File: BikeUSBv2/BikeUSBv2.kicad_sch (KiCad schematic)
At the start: 50 parts, among them J1 TYPE-C-31-M-16, J2 Conn_01x02_Female, Q1 Q_NPN_BEC, SW1 SW_Push, SW2 SW_Push, U1 TPS63020DSJR, U2 ATtiny1616-M

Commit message: oops 2
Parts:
- D4, D5, D6, D7: footprint Diode_SMD:D_PowerDI-123 -> Diode_SMD:D_SOD-128
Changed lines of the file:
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@@
       (effects (font (size 1.27 1.27)) (justify left) hide)
     )
-    (property "Footprint" "Diode_SMD:D_PowerDI-123" (at 23.495 84.455 0)
+    (property "Footprint" "Diode_SMD:D_SOD-128" (at 23.495 84.455 0)
       (effects (font (size 1.27 1.27)) hide)
     )
@@
       (effects (font (size 1.27 1.27)) (justify left) hide)
     )
-    (property "Footprint" "Diode_SMD:D_PowerDI-123" (at 35.56 92.075 0)
+    (property "Footprint" "Diode_SMD:D_SOD-128" (at 35.56 92.075 0)
       (effects (font (size 1.27 1.27)) hide)
     )
@@
       (effects (font (size 1.27 1.27)) (justify left) hide)
     )
-    (property "Footprint" "Diode_SMD:D_PowerDI-123" (at 23.495 92.075 0)
+    (property "Footprint" "Diode_SMD:D_SOD-128" (at 23.495 92.075 0)
       (effects (font (size 1.27 1.27)) hide)
     )
@@
       (effects (font (size 1.27 1.27)) (justify left) hide)
     )
-    (property "Footprint" "Diode_SMD:D_PowerDI-123" (at 35.56 84.455 0)
-      (effects (font (size 1.27 1.27)) hide)
-    )
+    (property "Footprint" "Diode_SMD:D_SOD-128" (at 35.56 84.455 0)
+      (effects (font (size 1.27 1.27)) hide)
+    )

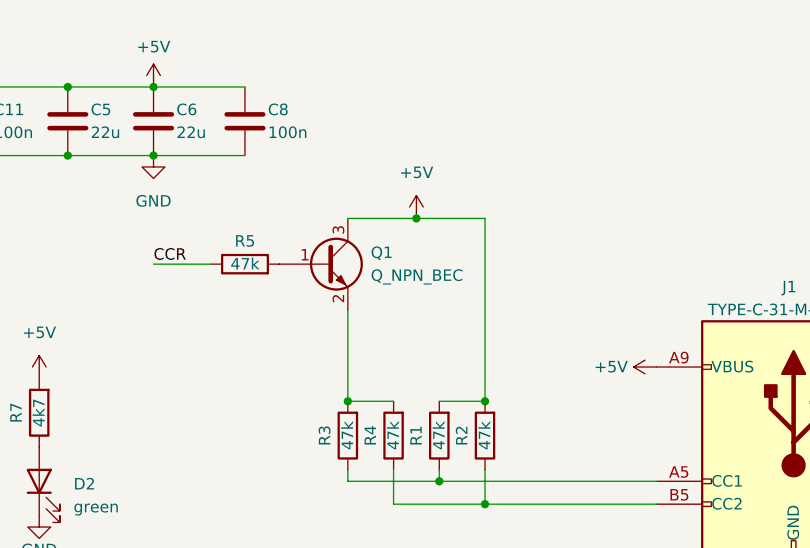
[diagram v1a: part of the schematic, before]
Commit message: NPN =/= PNP
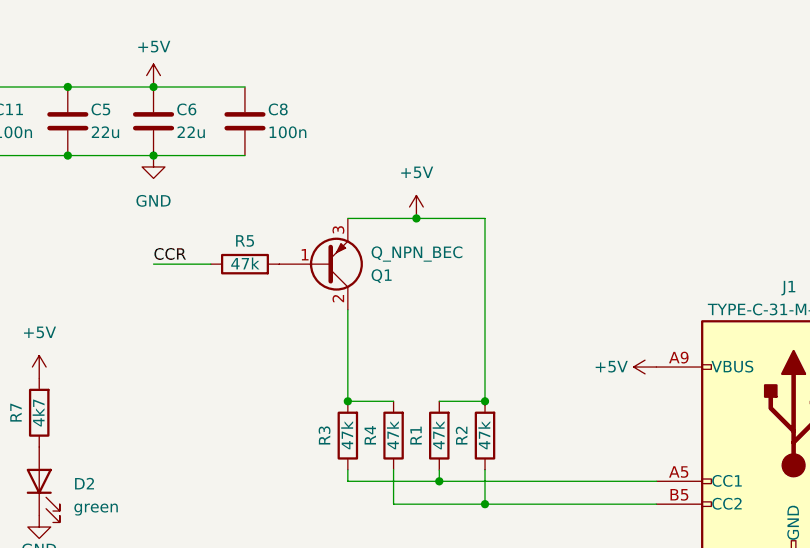
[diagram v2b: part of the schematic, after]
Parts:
- Q1: symbol Device:Q_NPN_BEC -> Device:Q_PNP_BCE
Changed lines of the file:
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@@
     )
   )
-  (symbol (lib_id "Device:Q_NPN_BEC") (at 157.48 73.66 0) (unit 1)
-    (in_bom yes) (on_board yes) (dnp no) (fields_autoplaced)
-    (property "Reference" "Q1" (at 162.56 72.39 0)
+  (symbol (lib_id "Device:Q_PNP_BCE") (at 157.48 73.66 0) (mirror x) (unit 1)
+    (in_bom yes) (on_board yes) (dnp no)
+    (property "Reference" "Q1" (at 162.56 74.93 0)
       (effects (font (size 1.27 1.27)) (justify left))
     )
-    (property "Value" "Q_NPN_BEC" (at 162.56 74.93 0)
+    (property "Value" "Q_NPN_BEC" (at 162.56 72.39 0)
       (effects (font (size 1.27 1.27)) (justify left))
     )
-    (property "Footprint" "Package_TO_SOT_SMD:SOT-23_Handsoldering" (at 162.56 71.12 0)
+    (property "Footprint" "Package_TO_SOT_SMD:SOT-23_Handsoldering" (at 162.56 76.2 0)
       (effects (font (size 1.27 1.27)) hide)
     )

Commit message: update parts
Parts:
- C1, C10, C11, C8: LCSC (none) -> C1711
- C2, C3, C4: LCSC (none) -> C1779
- C5, C6, C7: LCSC (none) -> C12891
- C9: LCSC (none) -> C178661
- D4, D5, D6, D7: LCSC (none) -> C603062
- D8: LCSC (none) -> C7422622
- J1: LCSC (none) -> C283541
- L1: LCSC (none) -> C338840
- Q1: value Q_NPN_BEC -> MMBT3906; LCSC (none) -> C2891809; LCSC Part (none) -> C2891809
- R1, R10, R11, R2, R3, R4, R5: LCSC (none) -> C218592
- R12, R13, R14, R7, R8, R9: LCSC (none) -> C706357
- U1: LCSC (none) -> C15483
- U2: LCSC (none) -> C507118
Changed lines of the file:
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@@
+      (effects (font (size 1.27 1.27)) hide)
+    )
+    (property "LCSC" "C218592" (at 148.59 71.12 0)
       (effects (font (size 1.27 1.27)) hide)
     )
@@
       (effects (font (size 1.27 1.27)) hide)
     )
+    (property "LCSC" "C706357" (at 24.13 121.92 0)
+      (effects (font (size 1.27 1.27)) hide)
+    )
     (pin "1")
     (pin "2")
@@
       (effects (font (size 1.27 1.27)) hide)
     )
+    (property "LCSC" "C706357" (at 80.645 181.61 0)
+      (effects (font (size 1.27 1.27)) hide)
+    )
     (pin "1")
     (pin "2")
@@
       (effects (font (size 1.27 1.27)) (justify left))
     )
-    (property "Value" "Q_NPN_BEC" (at 162.56 72.39 0)
+    (property "Value" "MMBT3906" (at 162.56 72.39 0)
       (effects (font (size 1.27 1.27)) (justify left))
     )
@@
     )
     (property "Datasheet" "~" (at 157.48 73.66 0)
+      (effects (font (size 1.27 1.27)) hide)
+    )
+    (property "LCSC Part" "C2891809" (at 157.48 73.66 0)
+      (effects (font (size 1.27 1.27)) hide)
+    )
+    (property "LCSC" "C2891809" (at 162.56 74.93 0)
       (effects (font (size 1.27 1.27)) hide)
     )
@@
       (effects (font (size 1.27 1.27)) hide)
     )
+    (property "LCSC" "C603062" (at 25.4 84.455 0)
+      (effects (font (size 1.27 1.27)) hide)
+    )
     (pin "2")
     (pin "1")
@@
       (effects (font (size 1.27 1.27)) hide)
     )
+    (property "LCSC" "C7422622" (at 22.86 54.61 0)
+      (effects (font (size 1.27 1.27)) hide)
+    )
     (pin "1")
     (pin "2")
@@
     )
     (property "Sim.Pins" "1=K 2=A" (at 35.56 92.075 0)
+      (effects (font (size 1.27 1.27)) hide)
+    )
+    (property "LCSC" "C603062" (at 31.115 92.075 0)
       (effects (font (size 1.27 1.27)) hide)
     )
@@
       (effects (font (size 1.27 1.27)) hide)
     )
+    (property "LCSC" "C1711" (at 120.65 56.515 0)
+      (effects (font (size 1.27 1.27)) hide)
+    )
     (pin "1")
     (pin "2")
@@
     )
     (property "Datasheet" "https://www.usb.org/sites/default/files/documents/usb_type-c.zip" (at 209.55 92.71 0)
+      (effects (font (size 1.27 1.27)) hide)
+    )
+    (property "LCSC" "C283541" (at 208.28 76.2 0)
       (effects (font (size 1.27 1.27)) hide)
     )
@@
       (effects (font (size 1.27 1.27)) hide)
     )
+    (property "LCSC" "C1711" (at 55.245 95.25 0)
+      (effects (font (size 1.27 1.27)) hide)
+    )
     (pin "1")
     (pin "2")
@@
     )
     (property "Datasheet" "~" (at 77.47 118.745 0)
+      (effects (font (size 1.27 1.27)) hide)
+    )
+    (property "LCSC" "C218592" (at 74.93 118.745 0)
       (effects (font (size 1.27 1.27)) hide)
     )
@@
       (effects (font (size 1.27 1.27)) hide)
     )
+    (property "LCSC" "C1711" (at 66.04 59.69 0)
+      (effects (font (size 1.27 1.27)) hide)
+    )
     (pin "1")
     (pin "2")
@@
       (effects (font (size 1.27 1.27)) hide)
     )
+    (property "LCSC" "C603062" (at 25.4 92.075 0)
+      (effects (font (size 1.27 1.27)) hide)
+    )
     (pin "2")
     (pin "1")
@@
       (effects (font (size 1.27 1.27)) hide)
     )
+    (property "LCSC" "C1711" (at 151.13 56.515 0)
+      (effects (font (size 1.27 1.27)) hide)
+    )
     (pin "1")
     (pin "2")
@@
       (effects (font (size 1.27 1.27)) hide)
     )
+    (property "LCSC" "C218592" (at 157.48 92.71 0)
+      (effects (font (size 1.27 1.27)) hide)
+    )
     (pin "1")
     (pin "2")
@@
       (effects (font (size 1.27 1.27)) hide)
     )
+    (property "LCSC" "C706357" (at 80.645 173.99 0)
+      (effects (font (size 1.27 1.27)) hide)
+    )
     (pin "1")
     (pin "2")
@@
       (effects (font (size 1.27 1.27)) hide)
     )
+    (property "LCSC" "C338840" (at 74.295 97.79 0)
+      (effects (font (size 1.27 1.27)) hide)
+    )
     (pin "1")
     (pin "2")
@@
       (effects (font (size 1.27 1.27)) hide)
     )
+    (property "LCSC" "C218592" (at 172.72 92.71 0)
+      (effects (font (size 1.27 1.27)) hide)
+    )
     (pin "1")
     (pin "2")
@@
       (effects (font (size 1.27 1.27)) hide)
     )
+    (property "LCSC" "C12891" (at 131.445 56.515 0)
+      (effects (font (size 1.27 1.27)) hide)
+    )
     (pin "1")
     (pin "2")
@@
       (effects (font (size 1.27 1.27)) hide)
     )
+    (property "LCSC" "C218592" (at 162.56 92.71 0)
+      (effects (font (size 1.27 1.27)) hide)
+    )
     (pin "1")
     (pin "2")
@@
     )
     (property "Datasheet" "~" (at 101.6 60.96 0)
+      (effects (font (size 1.27 1.27)) hide)
+    )
+    (property "LCSC" "C12891" (at 105.41 59.69 0)
       (effects (font (size 1.27 1.27)) hide)
     )
@@
     )
     (property "LCSC Part" "C15483" (at 93.345 120.015 0)
+      (effects (font (size 1.27 1.27)) hide)
+    )
+    (property "LCSC" "C15483" (at 93.345 76.835 0)
       (effects (font (size 1.27 1.27)) hide)
     )
@@
     )
     (property "Datasheet" "http://ww1.microchip.com/downloads/en/DeviceDoc/ATtiny3216_ATtiny1616-data-sheet-40001997B.pdf" (at 55.88 163.83 0)
+      (effects (font (size 1.27 1.27)) hide)
+    )
+    (property "LCSC" "C507118" (at 58.0741 138.43 0)
       (effects (font (size 1.27 1.27)) hide)
     )
@@
       (effects (font (size 1.27 1.27)) hide)
     )
+    (property "LCSC" "C1779" (at 85.09 59.69 0)
+      (effects (font (size 1.27 1.27)) hide)
+    )
     (pin "1")
     (pin "2")
@@
       (effects (font (size 1.27 1.27)) hide)
     )
+    (property "LCSC" "C218592" (at 114.3 86.995 0)
+      (effects (font (size 1.27 1.27)) hide)
+    )
     (pin "1")
     (pin "2")
@@
       (effects (font (size 1.27 1.27)) hide)
     )
+    (property "LCSC" "C706357" (at 74.93 126.365 0)
+      (effects (font (size 1.27 1.27)) hide)
+    )
     (pin "1")
     (pin "2")
@@
     )
     (property "Datasheet" "~" (at 116.84 94.615 0)
+      (effects (font (size 1.27 1.27)) hide)
+    )
+    (property "LCSC" "C706357" (at 114.3 94.615 0)
       (effects (font (size 1.27 1.27)) hide)
     )
@@
     )
     (property "Sim.Pins" "1=K 2=A" (at 35.56 84.455 0)
+      (effects (font (size 1.27 1.27)) hide)
+    )
+    (property "LCSC" "C603062" (at 31.115 84.455 0)
       (effects (font (size 1.27 1.27)) hide)
     )
@@
       (effects (font (size 1.27 1.27)) hide)
     )
+    (property "LCSC" "C1779" (at 75.565 59.69 0)
+      (effects (font (size 1.27 1.27)) hide)
+    )
     (pin "1")
     (pin "2")
@@
       (effects (font (size 1.27 1.27)) hide)
     )
+    (property "LCSC" "C706357" (at 123.19 90.17 0)
+      (effects (font (size 1.27 1.27)) hide)
+    )
     (pin "1")
     (pin "2")
@@
     )
     (property "Datasheet" "~" (at 138.43 57.785 0)
+      (effects (font (size 1.27 1.27)) hide)
+    )
+    (property "LCSC" "C12891" (at 140.97 56.515 0)
       (effects (font (size 1.27 1.27)) hide)
     )
@@
       (effects (font (size 1.27 1.27)) hide)
     )
+    (property "LCSC" "C178661" (at 48.26 70.231 0)
+      (effects (font (size 1.27 1.27)) hide)
+    )
     (pin "1")
     (pin "2")
@@
       (effects (font (size 1.27 1.27)) hide)
     )
+    (property "LCSC" "C218592" (at 167.64 92.71 0)
+      (effects (font (size 1.27 1.27)) hide)
+    )
     (pin "1")
     (pin "2")
@@
       (effects (font (size 1.27 1.27)) hide)
     )
+    (property "LCSC" "C1779" (at 94.615 59.69 0)
+      (effects (font (size 1.27 1.27)) hide)
+    )

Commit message: dingsbumbs
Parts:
- C1, C10, C11, C8: LCSC C1711 -> (none)
- C2, C3, C4: LCSC C1779 -> (none)
- C5, C6, C7: LCSC C12891 -> (none)
- C9: LCSC C178661 -> (none)
- D10: value CMS04(TE12L,Q,M) -> ~
- D4, D5, D6, D7: LCSC C603062 -> (none)
- D8: LCSC C7422622 -> (none)
- J1: LCSC C283541 -> (none)
- L1: LCSC C338840 -> (none)
- Q1: LCSC C2891809 -> (none)
- R1, R10, R11, R2, R3, R4, R5: LCSC C218592 -> (none)
- R12, R13, R14, R7, R8, R9: LCSC C706357 -> (none)
- U1: LCSC C15483 -> (none)
- U2: LCSC C507118 -> (none)
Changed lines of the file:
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@@
-      (effects (font (size 1.27 1.27)) hide)
-    )
-    (property "LCSC" "C218592" (at 148.59 71.12 0)
       (effects (font (size 1.27 1.27)) hide)
     )
@@
       (effects (font (size 1.27 1.27)) hide)
     )
-    (property "LCSC" "C706357" (at 24.13 121.92 0)
-      (effects (font (size 1.27 1.27)) hide)
-    )
     (pin "1")
     (pin "2")
@@
       (effects (font (size 1.27 1.27)) (justify left))
     )
-    (property "Value" "CMS04(TE12L,Q,M)" (at 81.915 127.635 90)
+    (property "Value" "~" (at 81.915 127.635 90)
       (effects (font (size 1.27 1.27)) (justify left) hide)
     )
@@
       (effects (font (size 1.27 1.27)) hide)
     )
-    (property "LCSC" "C706357" (at 80.645 181.61 0)
-      (effects (font (size 1.27 1.27)) hide)
-    )
     (pin "1")
     (pin "2")
@@
     )
     (property "LCSC Part" "C2891809" (at 157.48 73.66 0)
-      (effects (font (size 1.27 1.27)) hide)
-    )
-    (property "LCSC" "C2891809" (at 162.56 74.93 0)
       (effects (font (size 1.27 1.27)) hide)
     )
@@
       (effects (font (size 1.27 1.27)) hide)
     )
-    (property "LCSC" "C603062" (at 25.4 84.455 0)
-      (effects (font (size 1.27 1.27)) hide)
-    )
     (pin "2")
     (pin "1")
@@
       (effects (font (size 1.27 1.27)) hide)
     )
-    (property "LCSC" "C7422622" (at 22.86 54.61 0)
-      (effects (font (size 1.27 1.27)) hide)
-    )
     (pin "1")
     (pin "2")
@@
     )
     (property "Sim.Pins" "1=K 2=A" (at 35.56 92.075 0)
-      (effects (font (size 1.27 1.27)) hide)
-    )
-    (property "LCSC" "C603062" (at 31.115 92.075 0)
       (effects (font (size 1.27 1.27)) hide)
     )
@@
       (effects (font (size 1.27 1.27)) hide)
     )
-    (property "LCSC" "C1711" (at 120.65 56.515 0)
-      (effects (font (size 1.27 1.27)) hide)
-    )
     (pin "1")
     (pin "2")
@@
     )
     (property "Datasheet" "https://www.usb.org/sites/default/files/documents/usb_type-c.zip" (at 209.55 92.71 0)
-      (effects (font (size 1.27 1.27)) hide)
-    )
-    (property "LCSC" "C283541" (at 208.28 76.2 0)
       (effects (font (size 1.27 1.27)) hide)
     )
@@
       (effects (font (size 1.27 1.27)) hide)
     )
-    (property "LCSC" "C1711" (at 55.245 95.25 0)
-      (effects (font (size 1.27 1.27)) hide)
-    )
     (pin "1")
     (pin "2")
@@
     )
     (property "Datasheet" "~" (at 77.47 118.745 0)
-      (effects (font (size 1.27 1.27)) hide)
-    )
-    (property "LCSC" "C218592" (at 74.93 118.745 0)
       (effects (font (size 1.27 1.27)) hide)
     )
@@
       (effects (font (size 1.27 1.27)) hide)
     )
-    (property "LCSC" "C1711" (at 66.04 59.69 0)
-      (effects (font (size 1.27 1.27)) hide)
-    )
     (pin "1")
     (pin "2")
@@
       (effects (font (size 1.27 1.27)) hide)
     )
-    (property "LCSC" "C603062" (at 25.4 92.075 0)
-      (effects (font (size 1.27 1.27)) hide)
-    )
     (pin "2")
     (pin "1")
@@
       (effects (font (size 1.27 1.27)) hide)
     )
-    (property "LCSC" "C1711" (at 151.13 56.515 0)
-      (effects (font (size 1.27 1.27)) hide)
-    )
     (pin "1")
     (pin "2")
@@
       (effects (font (size 1.27 1.27)) hide)
     )
-    (property "LCSC" "C218592" (at 157.48 92.71 0)
-      (effects (font (size 1.27 1.27)) hide)
-    )
     (pin "1")
     (pin "2")
@@
       (effects (font (size 1.27 1.27)) hide)
     )
-    (property "LCSC" "C706357" (at 80.645 173.99 0)
-      (effects (font (size 1.27 1.27)) hide)
-    )
     (pin "1")
     (pin "2")
@@
       (effects (font (size 1.27 1.27)) hide)
     )
-    (property "LCSC" "C338840" (at 74.295 97.79 0)
-      (effects (font (size 1.27 1.27)) hide)
-    )
     (pin "1")
     (pin "2")
@@
       (effects (font (size 1.27 1.27)) hide)
     )
-    (property "LCSC" "C218592" (at 172.72 92.71 0)
-      (effects (font (size 1.27 1.27)) hide)
-    )
     (pin "1")
     (pin "2")
@@
       (effects (font (size 1.27 1.27)) hide)
     )
-    (property "LCSC" "C12891" (at 131.445 56.515 0)
-      (effects (font (size 1.27 1.27)) hide)
-    )
     (pin "1")
     (pin "2")
@@
       (effects (font (size 1.27 1.27)) hide)
     )
-    (property "LCSC" "C218592" (at 162.56 92.71 0)
-      (effects (font (size 1.27 1.27)) hide)
-    )
     (pin "1")
     (pin "2")
@@
     )
     (property "Datasheet" "~" (at 101.6 60.96 0)
-      (effects (font (size 1.27 1.27)) hide)
-    )
-    (property "LCSC" "C12891" (at 105.41 59.69 0)
       (effects (font (size 1.27 1.27)) hide)
     )
@@
     )
     (property "LCSC Part" "C15483" (at 93.345 120.015 0)
-      (effects (font (size 1.27 1.27)) hide)
-    )
-    (property "LCSC" "C15483" (at 93.345 76.835 0)
       (effects (font (size 1.27 1.27)) hide)
     )
@@
     )
     (property "Datasheet" "http://ww1.microchip.com/downloads/en/DeviceDoc/ATtiny3216_ATtiny1616-data-sheet-40001997B.pdf" (at 55.88 163.83 0)
-      (effects (font (size 1.27 1.27)) hide)
-    )
-    (property "LCSC" "C507118" (at 58.0741 138.43 0)
       (effects (font (size 1.27 1.27)) hide)
     )
@@
       (effects (font (size 1.27 1.27)) hide)
     )
-    (property "LCSC" "C1779" (at 85.09 59.69 0)
-      (effects (font (size 1.27 1.27)) hide)
-    )
     (pin "1")
     (pin "2")
@@
       (effects (font (size 1.27 1.27)) hide)
     )
-    (property "LCSC" "C218592" (at 114.3 86.995 0)
-      (effects (font (size 1.27 1.27)) hide)
-    )
     (pin "1")
     (pin "2")
@@
       (effects (font (size 1.27 1.27)) hide)
     )
-    (property "LCSC" "C706357" (at 74.93 126.365 0)
-      (effects (font (size 1.27 1.27)) hide)
-    )
     (pin "1")
     (pin "2")
@@
     )
     (property "Datasheet" "~" (at 116.84 94.615 0)
-      (effects (font (size 1.27 1.27)) hide)
-    )
-    (property "LCSC" "C706357" (at 114.3 94.615 0)
       (effects (font (size 1.27 1.27)) hide)
     )
@@
     )
     (property "Sim.Pins" "1=K 2=A" (at 35.56 84.455 0)
-      (effects (font (size 1.27 1.27)) hide)
-    )
-    (property "LCSC" "C603062" (at 31.115 84.455 0)
       (effects (font (size 1.27 1.27)) hide)
     )
@@
       (effects (font (size 1.27 1.27)) hide)
     )
-    (property "LCSC" "C1779" (at 75.565 59.69 0)
-      (effects (font (size 1.27 1.27)) hide)
-    )
     (pin "1")
     (pin "2")
@@
       (effects (font (size 1.27 1.27)) hide)
     )
-    (property "LCSC" "C706357" (at 123.19 90.17 0)
-      (effects (font (size 1.27 1.27)) hide)
-    )
     (pin "1")
     (pin "2")
@@
     )
     (property "Datasheet" "~" (at 138.43 57.785 0)
-      (effects (font (size 1.27 1.27)) hide)
-    )
-    (property "LCSC" "C12891" (at 140.97 56.515 0)
       (effects (font (size 1.27 1.27)) hide)
     )
@@
       (effects (font (size 1.27 1.27)) hide)
     )
-    (property "LCSC" "C178661" (at 48.26 70.231 0)
-      (effects (font (size 1.27 1.27)) hide)
-    )
     (pin "1")
     (pin "2")
@@
       (effects (font (size 1.27 1.27)) hide)
     )
-    (property "LCSC" "C218592" (at 167.64 92.71 0)
-      (effects (font (size 1.27 1.27)) hide)
-    )
     (pin "1")
     (pin "2")
@@
       (effects (font (size 1.27 1.27)) hide)
     )
-    (property "LCSC" "C1779" (at 94.615 59.69 0)
-      (effects (font (size 1.27 1.27)) hide)
-    )
